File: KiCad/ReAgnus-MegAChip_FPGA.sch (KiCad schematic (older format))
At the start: 3 parts, among them J2 Conn_02x05_Odd_Even, U10 AS4C4M16SA, U7 GW1N-UV9LQ144

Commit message: more routing and placing components
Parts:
- added RN1: R_Pack04, Agnus:RESCAF80P320X160X60-8N, symbol Device:R_Pack04
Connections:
- net GND|NTSC_3V3 is gone; now on net DRA0_3V3|GND: U7.27 (IOL26A)
- net 3V3: now also RN1.5 (R4.2), RN1.6 (R3.2), RN1.7 (R2.2), RN1.8 (R1.2)
- net DONE: now also RN1.3 (R3.1)
- net DRA0_3V3|GND: no longer U7.26 (IOL22B)
- net DRA1|DRA0_3V3: now also U7.26 (IOL22B); no longer U7.25 (IOL22A)
- net DRA2|DRA1_3V3: now also U7.25 (IOL22A); no longer U7.24 (IOL15B/GCLKC_6)
- net READY: now also RN1.2 (R2.1)
- net RECONFIG_N: now also RN1.4 (R4.1)
- new net nNTSC_8372_3V3: RN1.1 (R1.1), U7.24 (IOL15B/GCLKC_6)
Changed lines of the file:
@@
 Text GLabel 5350 5950 3    50   BiDi ~ 0
 DRD15_3V3
-Text GLabel 1450 4600 0    50   Input ~ 0
-GND|NTSC_3V3
 Text GLabel 6350 4950 2    50   Input ~ 0
 A18_3V3
@@
 Text GLabel 1450 3500 0    50   Output ~ 0
 DRA3|DRA2_3V3
-Text GLabel 1450 4300 0    50   Output ~ 0
+Text GLabel 1450 4400 0    50   Output ~ 0
 DRA2|DRA1_3V3
-Text GLabel 1450 4400 0    50   Output ~ 0
+Text GLabel 1450 4500 0    50   Output ~ 0
 DRA1|DRA0_3V3
-Text GLabel 1450 4500 0    50   Output ~ 0
+Text GLabel 1450 4600 0    50   Output ~ 0
 DRA0_3V3|GND
 Text GLabel 2100 5950 3    50   Output ~ 0
@@
 Wire Wire Line
 	9350 5000 9450 5000
+Text GLabel 1450 4300 0    50   Input ~ 0
+nNTSC_8372_3V3
+$Comp
+L Device:R_Pack04 RN1
+U 1 1 6329F720
+P 9450 1300
+F 0 "RN1" H 9638 1346 50  0000 L CNN
+F 1 "R_Pack04" H 9638 1255 50  0000 L CNN
+F 2 "Agnus:RESCAF80P320X160X60-8N" V 9725 1300 50  0001 C CNN
+F 3 "~" H 9450 1300 50  0001 C CNN
+	1    9450 1300
+	1    0    0    -1
+$EndComp
+Text GLabel 9250 1100 1    50   Input ~ 0
+3V3
+Wire Wire Line
+	9250 1100 9350 1100
+Connection ~ 9350 1100
+Wire Wire Line
+	9350 1100 9450 1100
+Connection ~ 9450 1100
+Wire Wire Line
+	9450 1100 9550 1100
+Text GLabel 9550 1500 3    50   Input ~ 0
+RECONFIG_N
+Text GLabel 9450 1500 3    50   Input ~ 0
+DONE
+Text GLabel 9350 1500 3    50   Input ~ 0
+READY
+Text GLabel 9250 1500 3    50   Input ~ 0
+nNTSC_8372_3V3
 $EndSCHEMATC

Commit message: more routing and placing components
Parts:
- added RN2: R_Pack04, Agnus:RESCAF80P320X160X60-8N, symbol Device:R_Pack04
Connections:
- net GND: now also RN2.5 (R4.2), RN2.6 (R3.2), RN2.7 (R2.2), RN2.8 (R1.2)
- net MODE0: now also RN2.1 (R1.1)
- net MODE1: now also RN2.2 (R2.1)
- net TCK: now also RN2.3 (R3.1), RN2.4 (R4.1)
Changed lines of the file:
@@
 Text GLabel 9250 1500 3    50   Input ~ 0
 nNTSC_8372_3V3
+Text GLabel 10200 1100 1    50   Input ~ 0
+GND
+Text GLabel 10300 1500 3    50   Input ~ 0
+MODE1
+Text GLabel 10200 1500 3    50   Input ~ 0
+MODE0
+Text GLabel 10800 800  1    50   Input ~ 0
+3V3
+$Comp
+L Device:R_Pack04 RN2
+U 1 1 63318369
+P 10400 1300
+F 0 "RN2" H 10588 1346 50  0000 L CNN
+F 1 "R_Pack04" H 10588 1255 50  0000 L CNN
+F 2 "Agnus:RESCAF80P320X160X60-8N" V 10675 1300 50  0001 C CNN
+F 3 "~" H 10400 1300 50  0001 C CNN
+	1    10400 1300
+	1    0    0    -1
+$EndComp
+Text GLabel 10700 800  1    50   Input ~ 0
+3V3
+Wire Wire Line
+	10200 1100 10300 1100
+Connection ~ 10300 1100
+Wire Wire Line
+	10300 1100 10400 1100
+Connection ~ 10400 1100
+Wire Wire Line
+	10400 1100 10500 1100
+Text GLabel 10400 1500 3    50   Input ~ 0
+TCK
+Wire Wire Line
+	10400 1500 10500 1500
 $EndSCHEMATC

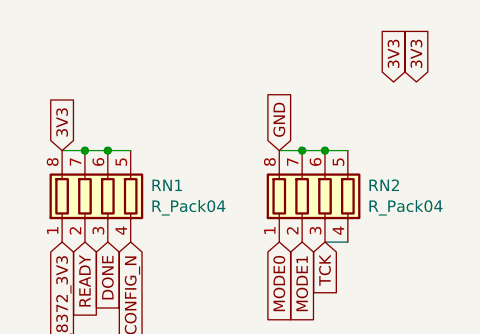
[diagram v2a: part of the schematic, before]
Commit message: renaming of Capacitors
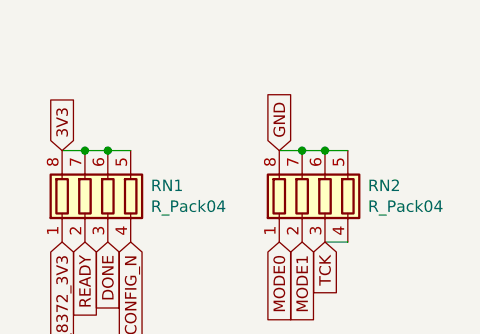
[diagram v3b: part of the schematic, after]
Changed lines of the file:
@@
 Text GLabel 10200 1500 3    50   Input ~ 0
 MODE0
-Text GLabel 10800 800  1    50   Input ~ 0
-3V3
 $Comp
 L Device:R_Pack04 RN2
@@
 	1    0    0    -1
 $EndComp
-Text GLabel 10700 800  1    50   Input ~ 0
-3V3
 Wire Wire Line
 	10200 1100 10300 1100

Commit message: more routing
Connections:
- net DRD0_3V3: now also U10.2 (DQ0); no longer U10.53 (DQ15)
- net DRD10_3V3: now also U10.45 (DQ10); no longer U10.4 (DQ1)
- net DRD11_3V3: now also U10.47 (DQ11); no longer U10.5 (DQ2)
- net DRD12_3V3: now also U10.48 (DQ12); no longer U10.7 (DQ3)
- net DRD13_3V3: now also U10.50 (DQ13); no longer U10.8 (DQ4)
- net DRD14_3V3: now also U10.51 (DQ14); no longer U10.10 (DQ5)
- net DRD15_3V3: now also U10.53 (DQ15); no longer U10.11 (DQ6)
- net DRD1_3V3: now also U10.4 (DQ1); no longer U10.51 (DQ14)
- net DRD2_3V3: now also U10.5 (DQ2); no longer U10.50 (DQ13)
- net DRD3_3V3: now also U10.7 (DQ3); no longer U10.48 (DQ12)
- net DRD4_3V3: now also U10.8 (DQ4); no longer U10.47 (DQ11)
- net DRD5_3V3: now also U10.10 (DQ5); no longer U10.45 (DQ10)
- net DRD6_3V3: now also U10.11 (DQ6); no longer U10.44 (DQ9)
- net DRD7_3V3: now also U10.13 (DQ7); no longer U10.42 (DQ8)
- net DRD8_3V3: now also U10.42 (DQ8); no longer U10.13 (DQ7)
- net DRD9_3V3: now also U10.44 (DQ9); no longer U10.2 (DQ0)
- net JP1: now also U7.142 (IOT8A)
- net A10_SDRAM: now reaches U10.22 (A10)
- net A10_SDRAM: now also U7.137 (IOT12B)
- net A0_SDRAM: now reaches U10.23 (A0)
- net A0_SDRAM: now also U7.138 (IOT12A)
- net A1_SDRAM: now reaches U10.24 (A1)
- net A1_SDRAM: now also U7.139 (IOT10B)
- net A2_SDRAM: now reaches U10.25 (A2)
- net A2_SDRAM: now also U7.140 (IOT10A)
- net A3_SDRAM: now reaches U10.26 (A3)
- net A3_SDRAM: now also U7.141 (IOT8B)
- net A4_SDRAM: now reaches U10.29 (A4)
- net A5_SDRAM: now reaches U10.30 (A5)
- net A6_SDRAM: now reaches U10.31 (A6)
- net A7_SDRAM: now reaches U10.32 (A7)
- net A8_SDRAM: now reaches U10.33 (A8)
- net A9_SDRAM: now reaches U10.34 (A9)
- net A11_SDRAM: now reaches U10.35 (A11)
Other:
- moved on the sheet: U10
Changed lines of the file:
@@
 L Memory_RAM:AS4C4M16SA U10
 U 1 1 632B4228
-P 9150 3700
-F 0 "U10" H 9150 5181 50  0000 C CNN
-F 1 "AS4C4M16SA" H 9150 5090 50  0000 C CNN
-F 2 "Package_SO:TSOP-II-54_22.2x10.16mm_P0.8mm" H 9150 3700 50  0001 C CIN
-F 3 "https://www.alliancememory.com/wp-content/uploads/pdf/dram/64M-AS4C4M16SA-CI_v3.0_March%202015.pdf" H 9150 3450 50  0001 C CNN
-	1    9150 3700
+P 9150 4000
+F 0 "U10" H 9150 5481 50  0000 C CNN
+F 1 "AS4C4M16SA" H 9150 5390 50  0000 C CNN
+F 2 "Package_SO:TSOP-II-54_22.2x10.16mm_P0.8mm" H 9150 4000 50  0001 C CIN
+F 3 "https://www.alliancememory.com/wp-content/uploads/pdf/dram/64M-AS4C4M16SA-CI_v3.0_March%202015.pdf" H 9150 3750 50  0001 C CNN
+	1    9150 4000
 	1    0    0    -1
 $EndComp
-Text GLabel 9950 4150 2    50   BiDi ~ 0
+Text GLabel 9950 2950 2    50   BiDi ~ 0
 DRD0_3V3
-Text GLabel 9950 4050 2    50   BiDi ~ 0
+Text GLabel 9950 3050 2    50   BiDi ~ 0
 DRD1_3V3
-Text GLabel 9950 3950 2    50   BiDi ~ 0
+Text GLabel 9950 3150 2    50   BiDi ~ 0
 DRD2_3V3
-Text GLabel 9950 3850 2    50   BiDi ~ 0
+Text GLabel 9950 3250 2    50   BiDi ~ 0
 DRD3_3V3
-Text GLabel 9950 3750 2    50   BiDi ~ 0
+Text GLabel 9950 3350 2    50   BiDi ~ 0
 DRD4_3V3
-Text GLabel 9950 3650 2    50   BiDi ~ 0
+Text GLabel 9950 3450 2    50   BiDi ~ 0
 DRD5_3V3
 Text GLabel 9950 3550 2    50   BiDi ~ 0
 DRD6_3V3
-Text GLabel 9950 3450 2    50   BiDi ~ 0
+Text GLabel 9950 3650 2    50   BiDi ~ 0
 DRD7_3V3
-Text GLabel 9950 3350 2    50   BiDi ~ 0
+Text GLabel 9950 3750 2    50   BiDi ~ 0
 DRD8_3V3
-Text GLabel 9950 2650 2    50   BiDi ~ 0
+Text GLabel 9950 3850 2    50   BiDi ~ 0
 DRD9_3V3
-Text GLabel 9950 2750 2    50   BiDi ~ 0
+Text GLabel 9950 3950 2    50   BiDi ~ 0
 DRD10_3V3
-Text GLabel 9950 2850 2    50   BiDi ~ 0
+Text GLabel 9950 4050 2    50   BiDi ~ 0
 DRD11_3V3
-Text GLabel 9950 2950 2    50   BiDi ~ 0
+Text GLabel 9950 4150 2    50   BiDi ~ 0
 DRD12_3V3
-Text GLabel 9950 3050 2    50   BiDi ~ 0
+Text GLabel 9950 4250 2    50   BiDi ~ 0
 DRD13_3V3
-Text GLabel 9950 3150 2    50   BiDi ~ 0
+Text GLabel 9950 4350 2    50   BiDi ~ 0
 DRD14_3V3
-Text GLabel 9950 3250 2    50   BiDi ~ 0
+Text GLabel 9950 4450 2    50   BiDi ~ 0
 DRD15_3V3
-Text GLabel 8850 2400 1    50   Input ~ 0
+Text GLabel 8850 2700 1    50   Input ~ 0
 3V3
 Wire Wire Line
-	8850 2400 8950 2400
-Connection ~ 8950 2400
+	8850 2700 8950 2700
+Connection ~ 8950 2700
 Wire Wire Line
-	8950 2400 9050 2400
-Connection ~ 9050 2400
+	8950 2700 9050 2700
+Connection ~ 9050 2700
 Wire Wire Line
-	9050 2400 9150 2400
-Connection ~ 9150 2400
+	9050 2700 9150 2700
+Connection ~ 9150 2700
 Wire Wire Line
-	9150 2400 9250 2400
-Connection ~ 9250 2400
+	9150 2700 9250 2700
+Connection ~ 9250 2700
 Wire Wire Line
-	9250 2400 9350 2400
-Connection ~ 9350 2400
+	9250 2700 9350 2700
+Connection ~ 9350 2700
 Wire Wire Line
-	9350 2400 9450 2400
-Text GLabel 8850 5000 3    50   Input ~ 0
+	9350 2700 9450 2700
+Text GLabel 8850 5300 3    50   Input ~ 0
 GND
 Wire Wire Line
-	8850 5000 8950 5000
-Connection ~ 8950 5000
+	8850 5300 8950 5300
+Connection ~ 8950 5300
 Wire Wire Line
-	8950 5000 9050 5000
-Connection ~ 9050 5000
+	8950 5300 9050 5300
+Connection ~ 9050 5300
 Wire Wire Line
-	9050 5000 9150 5000
-Connection ~ 9150 5000
+	9050 5300 9150 5300
+Connection ~ 9150 5300
 Wire Wire Line
-	9150 5000 9250 5000
-Connection ~ 9250 5000
+	9150 5300 9250 5300
+Connection ~ 9250 5300
 Wire Wire Line
-	9250 5000 9350 5000
-Connection ~ 9350 5000
+	9250 5300 9350 5300
+Connection ~ 9350 5300
 Wire Wire Line
-	9350 5000 9450 5000
+	9350 5300 9450 5300
 Text GLabel 1450 4300 0    50   Input ~ 0
 nNTSC_8372_3V3
@@
 Wire Wire Line
 	10400 1500 10500 1500
+Text GLabel 8350 2950 0    50   Input ~ 0
+A0_SDRAM
+Text GLabel 8350 3050 0    50   Input ~ 0
+A1_SDRAM
+Text GLabel 8350 3150 0    50   Input ~ 0
+A2_SDRAM
+Text GLabel 8350 3250 0    50   Input ~ 0
+A3_SDRAM
+Text GLabel 8350 3350 0    50   Input ~ 0
+A4_SDRAM
+Text GLabel 8350 3450 0    50   Input ~ 0
+A5_SDRAM
+Text GLabel 8350 3550 0    50   Input ~ 0
+A6_SDRAM
+Text GLabel 8350 3650 0    50   Input ~ 0
+A7_SDRAM
+Text GLabel 8350 3750 0    50   Input ~ 0
+A8_SDRAM
+Text GLabel 8350 3850 0    50   Input ~ 0
+A9_SDRAM
+Text GLabel 8350 3950 0    50   Input ~ 0
+A10_SDRAM
+Text GLabel 8350 4050 0    50   Input ~ 0
+A11_SDRAM
+Text GLabel 4050 1050 1    50   Output ~ 0
+A0_SDRAM
+Text GLabel 3950 1050 1    50   Output ~ 0
+A1_SDRAM
+Text GLabel 3850 1050 1    50   Output ~ 0
+A2_SDRAM
+Text GLabel 3750 1050 1    50   Output ~ 0
+A3_SDRAM
+Text GLabel 5100 900  1    50   Output ~ 0
+A4_SDRAM
+Text GLabel 5450 900  1    50   Output ~ 0
+A5_SDRAM
+Text GLabel 5550 900  1    50   Output ~ 0
+A6_SDRAM
+Text GLabel 5650 900  1    50   Output ~ 0
+A7_SDRAM
+Text GLabel 5750 900  1    50   Output ~ 0
+A8_SDRAM
+Text GLabel 5850 900  1    50   Output ~ 0
+A9_SDRAM
+Text GLabel 4150 1050 1    50   Output ~ 0
+A10_SDRAM
+Text GLabel 4950 900  1    50   Output ~ 0
+A11_SDRAM
+Text GLabel 3650 1050 1    50   Input ~ 0
+JP1
 $EndSCHEMATC

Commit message: more routing
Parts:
- added J1: Conn_02x02_Odd_Even, Connector_PinHeader_2.00mm:PinHeader_2x02_P2.00mm_Vertical, symbol Connector_Generic:Conn_02x02_Odd_Even
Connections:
- net GCLKT_1 is gone; now on net CLK_SDRAM: U7.123 (GCLKT_1/IOT29A)
- net A11_SDRAM: now also U7.126 (IOT24B)
- net A4_SDRAM: now also U7.133 (IOT17B)
- net A5_SDRAM: now also U7.132 (IOT20A)
- net A6_SDRAM: now also U7.131 (IOT20B)
- net A7_SDRAM: now also U7.130 (IOT22A)
- net A8_SDRAM: now also U7.129 (IOT22B)
- net A9_SDRAM: now also U7.128 (IOT24A)
- net DQML_SDRAM: now reaches U10.15 (DQML)
- net DQML_SDRAM: now also U7.120 (IOT32B)
- net WE_SDRAM: now reaches U10.16 (~WE~)
- net WE_SDRAM: now also U7.121 (IOT32A)
- net CAS_SDRAM: now reaches U10.17 (~CAS~)
- net CAS_SDRAM: now also U7.124 (IOT27B)
- net RAS_SDRAM: now reaches U10.18 (~RAS~)
- net RAS_SDRAM: now also U7.125 (IOT27A)
- net CS_SDRAM: now reaches U10.19 (~CS~)
- net CS_SDRAM: now also U7.134 (IOT17A)
- net BA0_SDRAM: now reaches U10.20 (BA0)
- net BA0_SDRAM: now also U7.135 (IOT15B)
- net BA1_SDRAM: now reaches U10.21 (BA1)
- net BA1_SDRAM: now also U7.136 (IOT15A)
- net CKE_SDRAM: now reaches U10.37 (CKE)
- net CKE_SDRAM: now also U7.122 (GCLKC_1/IOT29B)
- net CLK_SDRAM: now reaches U10.38 (CLK)
- net DQMH_SDRAM: now reaches U10.39 (DQMH)
- net DQMH_SDRAM: now also U7.119 (IOT34A)
- new net A20: J1.1 (Pin_1)
- new net A21: J1.3 (Pin_3)
- new net A22: J1.2 (Pin_2)
- new net A23: J1.4 (Pin_4)
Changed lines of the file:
@@
 Text GLabel 3800 5950 3    50   Input ~ 0
 GCLKT_4
-Text GLabel 6350 1600 2    50   Input ~ 0
-GCLKT_1
 Text GLabel 3550 1050 1    50   Input ~ 0
 MODE1
@@
 Text GLabel 3750 1050 1    50   Output ~ 0
 A3_SDRAM
-Text GLabel 5100 900  1    50   Output ~ 0
+Text GLabel 4550 1050 1    50   Output ~ 0
 A4_SDRAM
-Text GLabel 5450 900  1    50   Output ~ 0
+Text GLabel 4650 1050 1    50   Output ~ 0
 A5_SDRAM
-Text GLabel 5550 900  1    50   Output ~ 0
+Text GLabel 4750 1050 1    50   Output ~ 0
 A6_SDRAM
-Text GLabel 5650 900  1    50   Output ~ 0
+Text GLabel 4850 1050 1    50   Output ~ 0
 A7_SDRAM
-Text GLabel 5750 900  1    50   Output ~ 0
+Text GLabel 4950 1050 1    50   Output ~ 0
 A8_SDRAM
-Text GLabel 5850 900  1    50   Output ~ 0
+Text GLabel 5050 1050 1    50   Output ~ 0
 A9_SDRAM
 Text GLabel 4150 1050 1    50   Output ~ 0
 A10_SDRAM
-Text GLabel 4950 900  1    50   Output ~ 0
+Text GLabel 5150 1050 1    50   Output ~ 0
 A11_SDRAM
 Text GLabel 3650 1050 1    50   Input ~ 0
 JP1
+Text GLabel 8350 4200 0    50   Input ~ 0
+BA0_SDRAM
+Text GLabel 8350 4300 0    50   Input ~ 0
+BA1_SDRAM
+Text GLabel 4350 1050 1    50   Output ~ 0
+BA0_SDRAM
+Text GLabel 4250 1050 1    50   Output ~ 0
+BA1_SDRAM
+Text GLabel 8350 4450 0    50   Input ~ 0
+CLK_SDRAM
+Text GLabel 8350 4550 0    50   Input ~ 0
+CKE_SDRAM
+Text GLabel 8350 5050 0    50   Input ~ 0
+CS_SDRAM
+Text GLabel 8350 4700 0    50   Input ~ 0
+RAS_SDRAM
+Text GLabel 8350 4800 0    50   Input ~ 0
+CAS_SDRAM
+Text GLabel 8350 4900 0    50   Input ~ 0
+WE_SDRAM
+Text GLabel 9950 4700 2    50   BiDi ~ 0
+DQML_SDRAM
+Text GLabel 9950 4800 2    50   BiDi ~ 0
+DQMH_SDRAM
+Text GLabel 4450 1050 1    50   Output ~ 0
+CS_SDRAM
+Text GLabel 5250 1050 1    50   Output ~ 0
+RAS_SDRAM
+Text GLabel 6350 1500 2    50   Output ~ 0
+CAS_SDRAM
+Text GLabel 6350 1800 2    50   Output ~ 0
+WE_SDRAM
+Text GLabel 6350 1900 2    50   BiDi ~ 0
+DQML_SDRAM
+Text GLabel 6350 1600 2    50   Output ~ 0
+CLK_SDRAM
+Text GLabel 6350 1700 2    50   Output ~ 0
+CKE_SDRAM
+Text GLabel 6350 2000 2    50   BiDi ~ 0
+DQMH_SDRAM
+Text GLabel 7000 1050 2    50   Input ~ 0
+A20
+Text GLabel 7000 950  2    50   Input ~ 0
+A21
+Text GLabel 7000 850  2    50   Input ~ 0
+A22
+Text GLabel 7000 750  2    50   Input ~ 0
+A23
+Text GLabel 8100 2350 2    50   Input ~ 0
+A22
+Text GLabel 8100 2450 2    50   Input ~ 0
+A23
+$Comp
+L Connector_Generic:Conn_02x02_Odd_Even J1
+U 1 1 636B90A6
+P 7800 2350
+F 0 "J1" H 7850 2567 50  0000 C CNN
+F 1 "Conn_02x02_Odd_Even" H 7850 2476 50  0000 C CNN
+F 2 "Connector_PinHeader_2.00mm:PinHeader_2x02_P2.00mm_Vertical" H 7800 2350 50  0001 C CNN
+F 3 "~" H 7800 2350 50  0001 C CNN
+	1    7800 2350
+	1    0    0    -1
+$EndComp
+Text GLabel 7600 2450 0    50   Input ~ 0
+A21
+Text GLabel 7600 2350 0    50   Input ~ 0
+A20
 $EndSCHEMATC

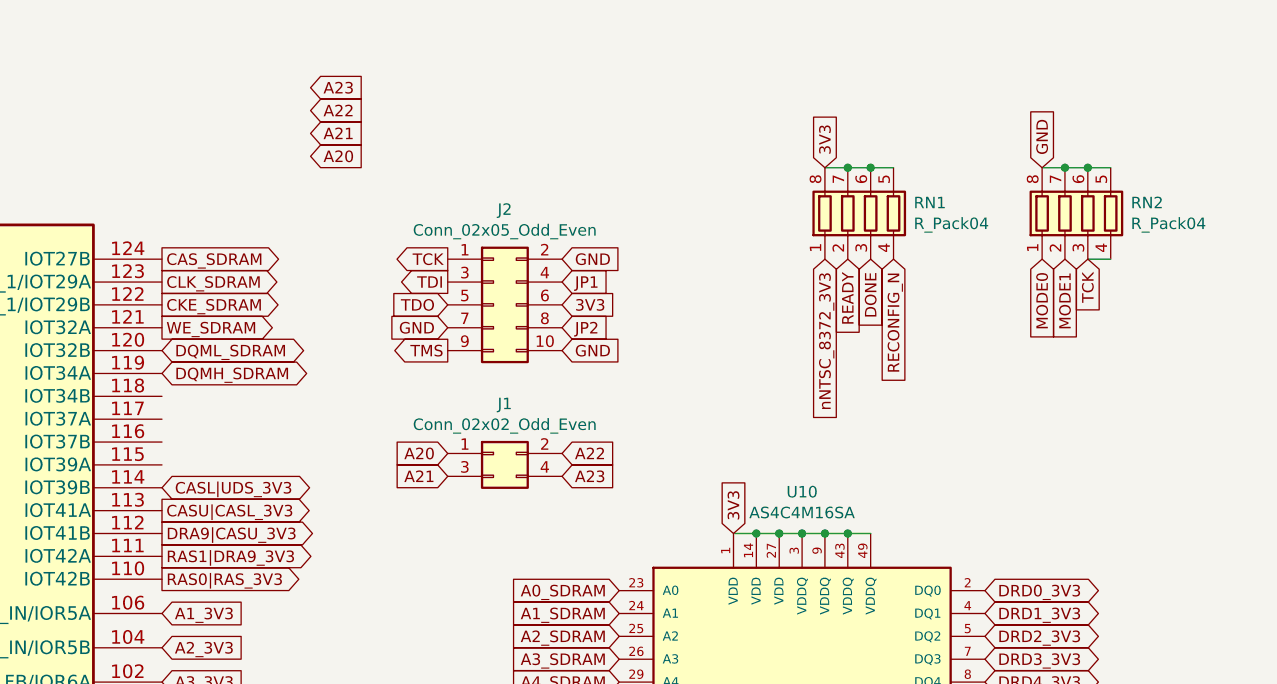
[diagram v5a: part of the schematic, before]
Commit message: added Oscillator X1 for SDRAM and GCLKT_1 pin on FPGA
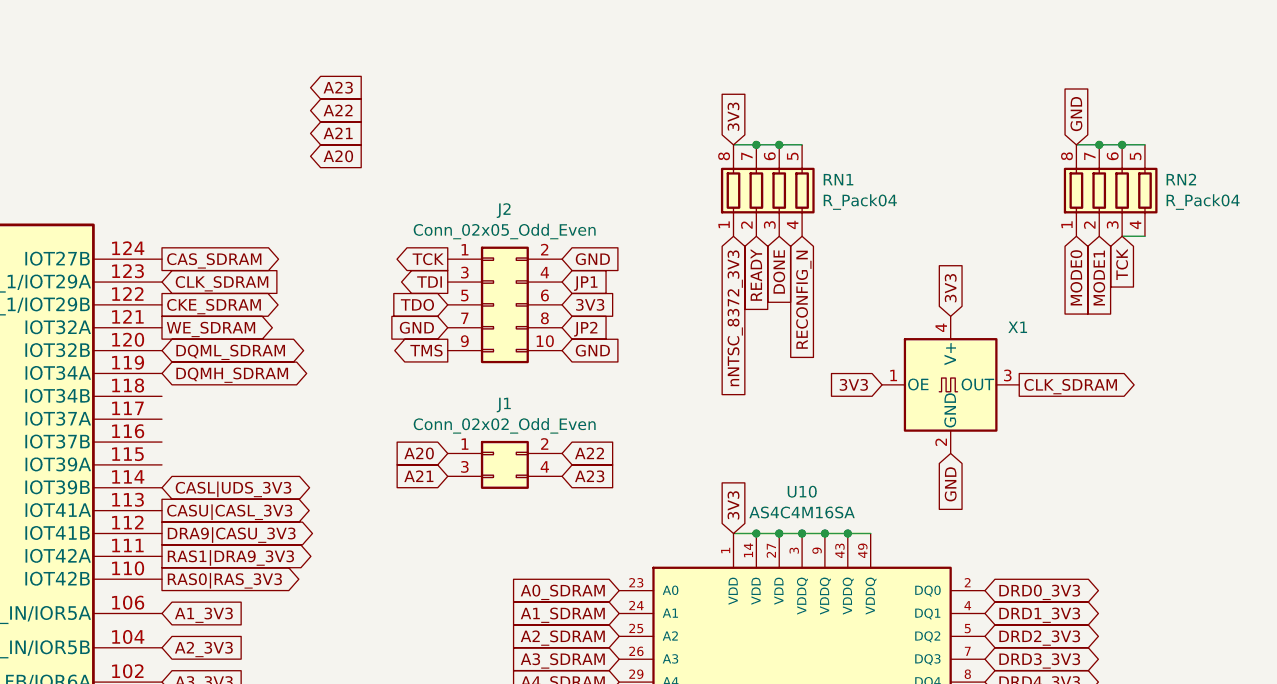
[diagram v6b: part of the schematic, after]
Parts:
- added X1: SG-8002CA, Oscillator:Oscillator_SMD_SeikoEpson_SG8002CA-4Pin_7.0x5.0mm, symbol Oscillator:SG-8002CA
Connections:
- net 3V3: now also X1.1 (OE), X1.4 (V+)
- net CLK_SDRAM: now also X1.3 (OUT)
- net GND: now also X1.2 (GND)
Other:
- moved on the sheet: RN1, RN2
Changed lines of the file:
@@
 L Device:R_Pack04 RN1
 U 1 1 6329F720
-P 9450 1300
-F 0 "RN1" H 9638 1346 50  0000 L CNN
-F 1 "R_Pack04" H 9638 1255 50  0000 L CNN
-F 2 "Agnus:RESCAF80P320X160X60-8N" V 9725 1300 50  0001 C CNN
-F 3 "~" H 9450 1300 50  0001 C CNN
-	1    9450 1300
+P 9050 1200
+F 0 "RN1" H 9238 1246 50  0000 L CNN
+F 1 "R_Pack04" H 9238 1155 50  0000 L CNN
+F 2 "Agnus:RESCAF80P320X160X60-8N" V 9325 1200 50  0001 C CNN
+F 3 "~" H 9050 1200 50  0001 C CNN
+	1    9050 1200
 	1    0    0    -1
 $EndComp
-Text GLabel 9250 1100 1    50   Input ~ 0
+Text GLabel 8850 1000 1    50   Input ~ 0
 3V3
 Wire Wire Line
-	9250 1100 9350 1100
-Connection ~ 9350 1100
+	8850 1000 8950 1000
+Connection ~ 8950 1000
 Wire Wire Line
-	9350 1100 9450 1100
-Connection ~ 9450 1100
+	8950 1000 9050 1000
+Connection ~ 9050 1000
 Wire Wire Line
-	9450 1100 9550 1100
-Text GLabel 9550 1500 3    50   Input ~ 0
+	9050 1000 9150 1000
+Text GLabel 9150 1400 3    50   Input ~ 0
 RECONFIG_N
-Text GLabel 9450 1500 3    50   Input ~ 0
+Text GLabel 9050 1400 3    50   Input ~ 0
 DONE
-Text GLabel 9350 1500 3    50   Input ~ 0
+Text GLabel 8950 1400 3    50   Input ~ 0
 READY
-Text GLabel 9250 1500 3    50   Input ~ 0
+Text GLabel 8850 1400 3    50   Input ~ 0
 nNTSC_8372_3V3
-Text GLabel 10200 1100 1    50   Input ~ 0
+Text GLabel 10350 1000 1    50   Input ~ 0
 GND
-Text GLabel 10300 1500 3    50   Input ~ 0
+Text GLabel 10450 1400 3    50   Input ~ 0
 MODE1
-Text GLabel 10200 1500 3    50   Input ~ 0
+Text GLabel 10350 1400 3    50   Input ~ 0
 MODE0
 $Comp
 L Device:R_Pack04 RN2
 U 1 1 63318369
-P 10400 1300
-F 0 "RN2" H 10588 1346 50  0000 L CNN
-F 1 "R_Pack04" H 10588 1255 50  0000 L CNN
-F 2 "Agnus:RESCAF80P320X160X60-8N" V 10675 1300 50  0001 C CNN
-F 3 "~" H 10400 1300 50  0001 C CNN
-	1    10400 1300
+P 10550 1200
+F 0 "RN2" H 10738 1246 50  0000 L CNN
+F 1 "R_Pack04" H 10738 1155 50  0000 L CNN
+F 2 "Agnus:RESCAF80P320X160X60-8N" V 10825 1200 50  0001 C CNN
+F 3 "~" H 10550 1200 50  0001 C CNN
+	1    10550 1200
 	1    0    0    -1
 $EndComp
 Wire Wire Line
-	10200 1100 10300 1100
-Connection ~ 10300 1100
+	10350 1000 10450 1000
+Connection ~ 10450 1000
 Wire Wire Line
-	10300 1100 10400 1100
-Connection ~ 10400 1100
+	10450 1000 10550 1000
+Connection ~ 10550 1000
 Wire Wire Line
-	10400 1100 10500 1100
-Text GLabel 10400 1500 3    50   Input ~ 0
+	10550 1000 10650 1000
+Text GLabel 10550 1400 3    50   Input ~ 0
 TCK
 Wire Wire Line
-	10400 1500 10500 1500
+	10550 1400 10650 1400
 Text GLabel 8350 2950 0    50   Input ~ 0
 A0_SDRAM
@@
 Text GLabel 6350 1900 2    50   BiDi ~ 0
 DQML_SDRAM
-Text GLabel 6350 1600 2    50   Output ~ 0
+Text GLabel 6350 1600 2    50   Input ~ 0
 CLK_SDRAM
 Text GLabel 6350 1700 2    50   Output ~ 0
@@
 Text GLabel 7600 2350 0    50   Input ~ 0
 A20
+$Comp
+L Oscillator:SG-8002CA X1
+U 1 1 636F2CC7
+P 9800 2050
+F 0 "X1" H 10050 2300 50  0000 L CNN
+F 1 "SG-8002CA" H 10144 2005 50  0001 L CNN
+F 2 "Oscillator:Oscillator_SMD_SeikoEpson_SG8002CA-4Pin_7.0x5.0mm" H 10500 1700 50  0001 C CNN
+F 3 "" H 9700 2050 50  0001 C CNN
+	1    9800 2050
+	1    0    0    -1
+$EndComp
+Text GLabel 9800 1750 1    50   Input ~ 0
+3V3
+Text GLabel 9500 2050 0    50   Input ~ 0
+3V3
+Text GLabel 9800 2350 3    50   Input ~ 0
+GND
+Text GLabel 10100 2050 2    50   Output ~ 0
+CLK_SDRAM
 $EndSCHEMATC
